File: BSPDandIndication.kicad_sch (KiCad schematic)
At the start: 50 parts, among them J1 Power12, J2 Masa, J3 12VTelem, J4 Sensors, J6 BSPD12OUT, K1 FINDER-36.11, Q1 BC817, U1 LM1117-5.0, U2 LM1117-5.0, U3 PIC12F629-IP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

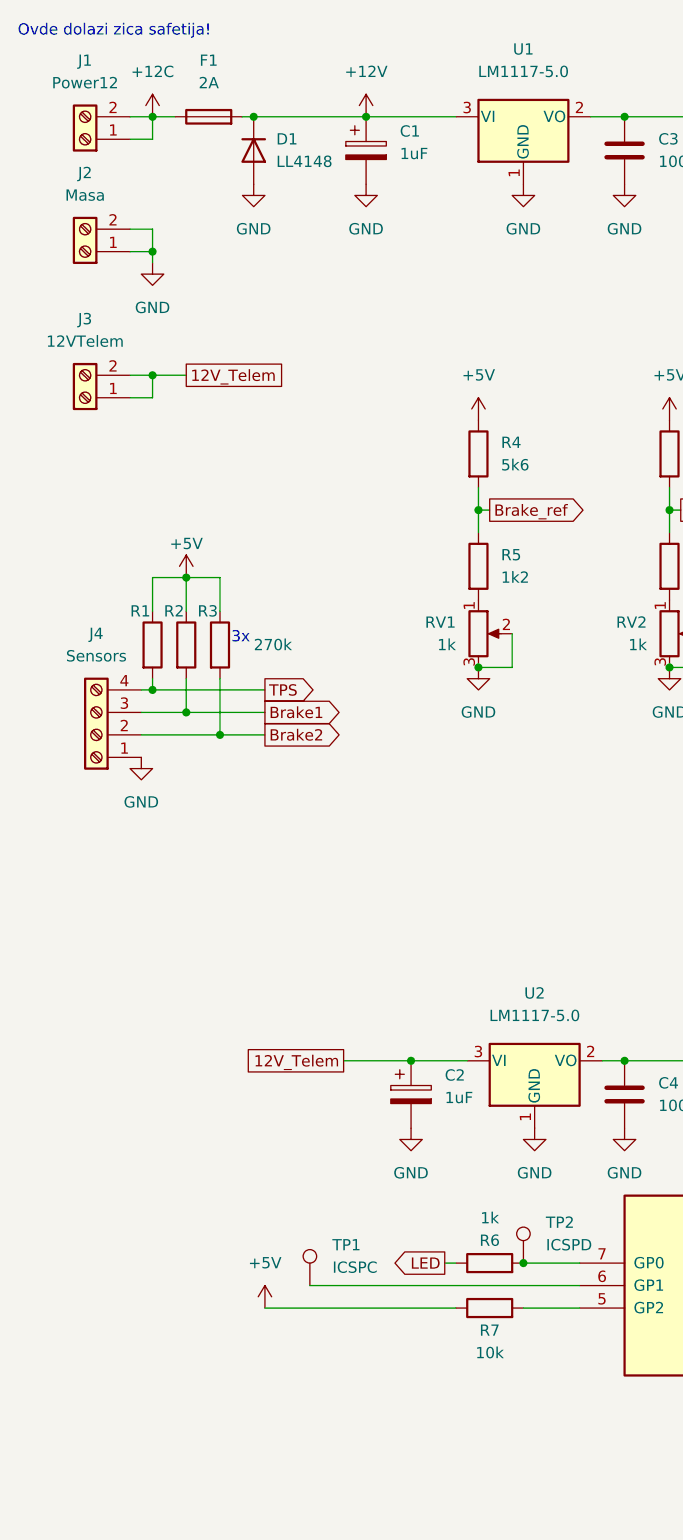
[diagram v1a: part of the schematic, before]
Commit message: Return safety pin (to recognize when safety fail)
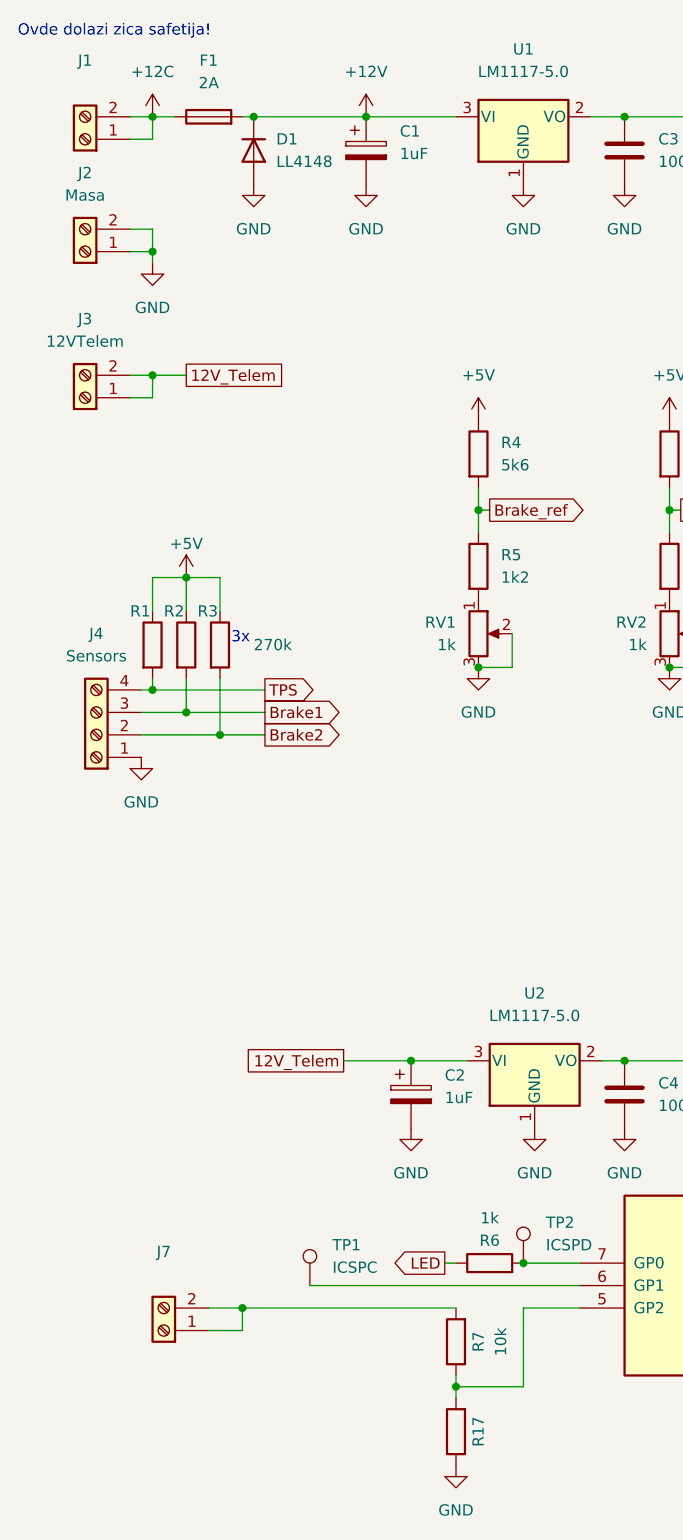
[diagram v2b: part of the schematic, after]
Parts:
- added J7: (no value), AK3001:AK300_1x02_P5.00mm_45-Degree, symbol Connector:Screw_Terminal_01x02
- added R17: (no value), Resistor_SMD:R_1206_3216Metric_Pad1.30x1.75mm_HandSolder, symbol Device:R
- J1: value Power12 -> (none)
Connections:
- net +5V: no longer R7.1
- net GND: now also R17.1
- net at U3.5 (GP2): now also R7.1, R17.2; no longer R7.2
- new net: J7.1 (Pin_1), J7.2 (Pin_2), R7.2
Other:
- moved on the sheet: R7
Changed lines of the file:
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@@
   (junction (at 83.82 25.4) (diameter 0) (color 0 0 0 0)
   )
+  (junction (at 40.64 160.02) (diameter 0) (color 0 0 0 0)
+  )
   (junction (at 30.48 25.4) (diameter 0) (color 0 0 0 0)
   )
@@
   (junction (at 207.01 129.54) (diameter 0) (color 0 0 0 0)
   )
+  (junction (at 64.77 168.91) (diameter 0) (color 0 0 0 0)
+  )
   (junction (at 120.65 91.44) (diameter 0) (color 0 0 0 0)
   )
@@
     (stroke (width 0) (type default) (color 0 0 0 0))
   )
+  (wire (pts (xy 40.64 160.02) (xy 64.77 160.02))
+    (stroke (width 0) (type default) (color 0 0 0 0))
+  )
   (wire (pts (xy 40.64 25.4) (xy 41.91 25.4))
     (stroke (width 0) (type default) (color 0 0 0 0))
@@
     (stroke (width 0) (type default) (color 0 0 0 0))
   )
+  (wire (pts (xy 64.77 168.91) (xy 64.77 170.18))
+    (stroke (width 0) (type default) (color 0 0 0 0))
+  )
   (wire (pts (xy 34.29 77.47) (xy 34.29 81.28))
     (stroke (width 0) (type default) (color 0 0 0 0))
   )
+  (wire (pts (xy 36.83 160.02) (xy 40.64 160.02))
+    (stroke (width 0) (type default) (color 0 0 0 0))
+  )
   (wire (pts (xy 30.48 38.1) (xy 30.48 40.64))
     (stroke (width 0) (type default) (color 0 0 0 0))
@@
     (stroke (width 0) (type default) (color 0 0 0 0))
   )
+  (wire (pts (xy 64.77 167.64) (xy 64.77 168.91))
+    (stroke (width 0) (type default) (color 0 0 0 0))
+  )
   (wire (pts (xy 88.9 67.31) (xy 88.9 69.85))
     (stroke (width 0) (type default) (color 0 0 0 0))
@@
     (stroke (width 0) (type default) (color 0 0 0 0))
   )
+  (wire (pts (xy 72.39 168.91) (xy 64.77 168.91))
+    (stroke (width 0) (type default) (color 0 0 0 0))
+  )
   (wire (pts (xy 144.78 31.75) (xy 158.75 31.75))
     (stroke (width 0) (type default) (color 0 0 0 0))
@@
     (stroke (width 0) (type default) (color 0 0 0 0))
   )
+  (wire (pts (xy 72.39 160.02) (xy 72.39 168.91))
+    (stroke (width 0) (type default) (color 0 0 0 0))
+  )
   (wire (pts (xy 93.98 142.24) (xy 93.98 132.08))
     (stroke (width 0) (type default) (color 0 0 0 0))
@@
     (stroke (width 0) (type default) (color 0 0 0 0))
   )
-  (wire (pts (xy 64.77 160.02) (xy 43.18 160.02))
-    (stroke (width 0) (type default) (color 0 0 0 0))
-  )
   (wire (pts (xy 255.27 133.35) (xy 251.46 133.35))
     (stroke (width 0) (type default) (color 0 0 0 0))
@@
     (stroke (width 0) (type default) (color 0 0 0 0))
   )
+  (wire (pts (xy 40.64 162.56) (xy 40.64 160.02))
+    (stroke (width 0) (type default) (color 0 0 0 0))
+  )
   (wire (pts (xy 30.48 27.94) (xy 30.48 25.4))
     (stroke (width 0) (type default) (color 0 0 0 0))
@@
   )
   (wire (pts (xy 127 96.52) (xy 129.54 96.52))
+    (stroke (width 0) (type default) (color 0 0 0 0))
+  )
+  (wire (pts (xy 36.83 162.56) (xy 40.64 162.56))
     (stroke (width 0) (type default) (color 0 0 0 0))
   )
@@
     (in_bom yes) (on_board yes) (fields_autoplaced)
     (property "Reference" "J1" (id 0) (at 22.86 19.05 0))
-    (property "Value" "Power12" (id 1) (at 22.86 21.59 0))
+    (property "Value" "" (id 1) (at 22.86 21.59 0))
     (property "Footprint" "AK3001:AK300_1x02_P5.00mm_45-Degree" (id 2) (at 22.86 27.94 0)
       (effects (font (size 1.27 1.27)) hide)
@@
   (symbol (lib_id "power:+5V") (at 158.75 86.36 0) (unit 1)
     (in_bom yes) (on_board yes) (fields_autoplaced)
-    (property "Reference" "#PWR?" (id 0) (at 158.75 90.17 0)
+    (property "Reference" "#PWR0134" (id 0) (at 158.75 90.17 0)
       (effects (font (size 1.27 1.27)) hide)
     )
@@
     (pin "4")
   )
-  (symbol (lib_id "Device:R") (at 68.58 160.02 90) (unit 1)
+  (symbol (lib_id "Device:R") (at 64.77 163.83 180) (unit 1)
     (in_bom yes) (on_board yes)
-    (property "Reference" "R7" (id 0) (at 68.58 162.56 90))
-    (property "Value" "10k" (id 1) (at 68.58 165.1 90))
-    (property "Footprint" "Resistor_SMD:R_1206_3216Metric_Pad1.30x1.75mm_HandSolder" (id 2) (at 68.58 161.798 90)
-      (effects (font (size 1.27 1.27)) hide)
-    )
-    (property "Datasheet" "~" (id 3) (at 68.58 160.02 0)
+    (property "Reference" "R7" (id 0) (at 67.31 163.83 90))
+    (property "Value" "10k" (id 1) (at 69.85 163.83 90))
+    (property "Footprint" "Resistor_SMD:R_1206_3216Metric_Pad1.30x1.75mm_HandSolder" (id 2) (at 66.548 163.83 90)
+      (effects (font (size 1.27 1.27)) hide)
+    )
+    (property "Datasheet" "~" (id 3) (at 64.77 163.83 0)
       (effects (font (size 1.27 1.27)) hide)
     )
@@
     (pin "3")
   )
+  (symbol (lib_id "Connector:Screw_Terminal_01x02") (at 31.75 162.56 180) (unit 1)
+    (in_bom yes) (on_board yes) (fields_autoplaced)
+    (property "Reference" "J7" (id 0) (at 31.75 153.67 0))
+    (property "Value" "" (id 1) (at 31.75 156.21 0))
+    (property "Footprint" "AK3001:AK300_1x02_P5.00mm_45-Degree" (id 2) (at 31.75 162.56 0)
+      (effects (font (size 1.27 1.27)) hide)
+    )
+    (property "Datasheet" "~" (id 3) (at 31.75 162.56 0)
+      (effects (font (size 1.27 1.27)) hide)
+    )
+    (pin "1")
+    (pin "2")
+  )
   (symbol (lib_id "Connector:TestPoint") (at 48.26 157.48 0) (unit 1)
     (in_bom yes) (on_board yes) (fields_autoplaced)
@@
     )
     (property "Datasheet" "~" (id 3) (at 53.34 157.48 0)
+      (effects (font (size 1.27 1.27)) hide)
+    )
+    (pin "1")
+  )
+  (symbol (lib_id "power:GND") (at 64.77 177.8 0) (unit 1)
+    (in_bom yes) (on_board yes) (fields_autoplaced)
+    (property "Reference" "#PWR0131" (id 0) (at 64.77 184.15 0)
+      (effects (font (size 1.27 1.27)) hide)
+    )
+    (property "Value" "GND" (id 1) (at 64.77 182.88 0))
+    (property "Footprint" "" (id 2) (at 64.77 177.8 0)
+      (effects (font (size 1.27 1.27)) hide)
+    )
+    (property "Datasheet" "" (id 3) (at 64.77 177.8 0)
       (effects (font (size 1.27 1.27)) hide)
     )
@@
     (pin "3")
     (pin "4")
-  )
-  (symbol (lib_id "power:+5V") (at 43.18 160.02 0) (unit 1)
-    (in_bom yes) (on_board yes) (fields_autoplaced)
-    (property "Reference" "#PWR0131" (id 0) (at 43.18 163.83 0)
-      (effects (font (size 1.27 1.27)) hide)
-    )
-    (property "Value" "+5V" (id 1) (at 43.18 154.94 0))
-    (property "Footprint" "" (id 2) (at 43.18 160.02 0)
-      (effects (font (size 1.27 1.27)) hide)
-    )
-    (property "Datasheet" "" (id 3) (at 43.18 160.02 0)
-      (effects (font (size 1.27 1.27)) hide)
-    )
-    (pin "1")
   )
   (symbol (lib_id "Connector:Screw_Terminal_01x02") (at 22.86 57.15 180) (unit 1)
@@
   (symbol (lib_id "power:GND") (at 158.75 101.6 0) (unit 1)
     (in_bom yes) (on_board yes) (fields_autoplaced)
-    (property "Reference" "#PWR?" (id 0) (at 158.75 107.95 0)
+    (property "Reference" "#PWR0135" (id 0) (at 158.75 107.95 0)
       (effects (font (size 1.27 1.27)) hide)
     )
@@
     (pin "1")
   )
+  (symbol (lib_id "Device:R") (at 64.77 173.99 180) (unit 1)
+    (in_bom yes) (on_board yes)
+    (property "Reference" "R17" (id 0) (at 67.31 173.99 90))
+    (property "Value" "" (id 1) (at 69.85 173.99 90))
+    (property "Footprint" "Resistor_SMD:R_1206_3216Metric_Pad1.30x1.75mm_HandSolder" (id 2) (at 66.548 173.99 90)
+      (effects (font (size 1.27 1.27)) hide)
+    )
+    (property "Datasheet" "~" (id 3) (at 64.77 173.99 0)
+      (effects (font (size 1.27 1.27)) hide)
+    )
+    (pin "1")
+    (pin "2")
+  )
   (symbol (lib_id "Connector:Screw_Terminal_01x02") (at 143.51 152.4 0) (unit 1)
     (in_bom yes) (on_board yes) (fields_autoplaced)
@@
       (reference "#PWR0130") (unit 1) (value "GND") (footprint "")
     )
-    (path "/aee6db03-4129-4d7f-a4de-0ab782209a2e"
-      (reference "#PWR0131") (unit 1) (value "+5V") (footprint "")
+    (path "/822678b3-4561-4f0b-a37b-5b437f0380f2"
+      (reference "#PWR0131") (unit 1) (value "GND") (footprint "")
     )
     (path "/7c831124-bf82-49cc-8f85-a19ef66f225e"
@@
     )
     (path "/5906882a-24ca-4f5c-88d6-aeaa0ee90b06"
-      (reference "#PWR?") (unit 1) (value "+5V") (footprint "")
+      (reference "#PWR0134") (unit 1) (value "+5V") (footprint "")
     )
     (path "/ce2cc115-5fb3-4d2b-849a-2e31b8eb22ed"
-      (reference "#PWR?") (unit 1) (value "GND") (footprint "")
+      (reference "#PWR0135") (unit 1) (value "GND") (footprint "")
     )
     (path "/2bd8ec9c-0097-430e-a5f3-2b204e671762"
@@
     )
     (path "/539be303-c3c5-402b-99d9-cc01b8a3aa7c"
-      (reference "J1") (unit 1) (value "Power12") (footprint "AK3001:AK300_1x02_P5.00mm_45-Degree")
+      (reference "J1") (unit 1) (value "SafetyIN") (footprint "AK3001:AK300_1x02_P5.00mm_45-Degree")
     )
     (path "/5fc74b98-5ae4-4d9a-b74f-82f6d013814f"
@@
       (reference "J6") (unit 1) (value "BSPD12OUT") (footprint "AK3001:AK300_1x02_P5.00mm_45-Degree")
     )
+    (path "/7cf0ce5f-75aa-4803-ba37-2350d8db80af"
+      (reference "J7") (unit 1) (value "SafetyReturn") (footprint "AK3001:AK300_1x02_P5.00mm_45-Degree")
+    )
     (path "/5705fd7f-e0d0-4535-a6ed-620e30f8044a"
       (reference "K1") (unit 1) (value "FINDER-36.11") (footprint "Relay_THT:Relay_SPDT_Finder_36.11")
@@
       (reference "R16") (unit 1) (value "1M") (footprint "Resistor_SMD:R_1206_3216Metric_Pad1.30x1.75mm_HandSolder")
     )
+    (path "/e845c67f-63bc-457d-b631-97c5abae1398"
+      (reference "R17") (unit 1) (value "4k7") (footprint "Resistor_SMD:R_1206_3216Metric_Pad1.30x1.75mm_HandSolder")
+    )
     (path "/17ed64e3-e6c6-4cc3-a283-72df321891f2"
       (reference "RV1") (unit 1) (value "1k") (footprint "Potentiometer_SMD:Potentiometer_Vishay_TS53YL_Vertical")
@@
     )
     (path "/647ee02d-4ca0-4bf9-bfab-6fa0d291e45c"
-      (reference "U4") (unit 5) (value "LM324") (footprint "")
+      (reference "U4") (unit 5) (value "LM324") (footprint "Package_SO:SO-14_3.9x8.65mm_P1.27mm")
     )
     (path "/4448d7e9-c20c-4211-890e-e9caf11189fc"
